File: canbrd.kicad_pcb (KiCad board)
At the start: 2 copper layers, 100 x 100 mm, 219 parts, among them J1 RP_DEBUG, J10 PwrOut, J11 IO2, J12 I^{2}C, J13 USB_C_Receptacle, J14 IO1, J15 IO0, J2 UPDI, J3 Micro_SD_Card, J4 GND, J5 Field24V, J6 Amphenol RJHSE5380, J7 Amphenol RJHSE5380, J8 CAN, J9 CAN, Q1 2N7002K, Q2 BSS83P, Q3 BSS83P, Q4 Q_PMOS_GDS, Q5 BC856, SW1 BOOTSEL, SW2 RESET, SW3 SW_DIP_x08, SW4 User, U1 W25Q16JVSNIQ, U10 ULN2003A, U11 ULN2003A, U12 MAX17634BATP+, U13 AP62250WU, U2 RP2040, U3 TJA1051T-3, U4 MCP2510-x/SO, U5 MAX3485CSA, U6 157119S12801, U8 157119S12801, U9 ATtiny427, Y1 12MHz, Y2 16MHz

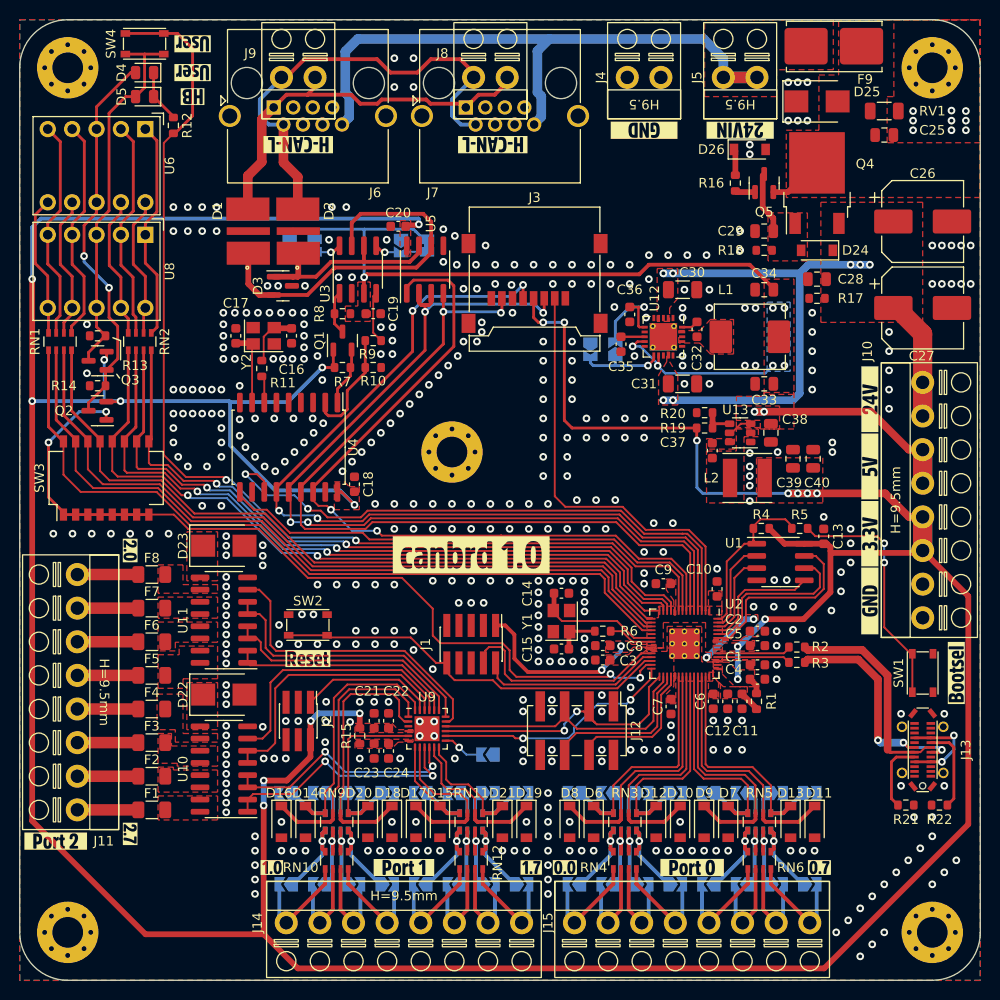
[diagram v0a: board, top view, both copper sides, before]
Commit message: rev1.1: Add I2C pullups
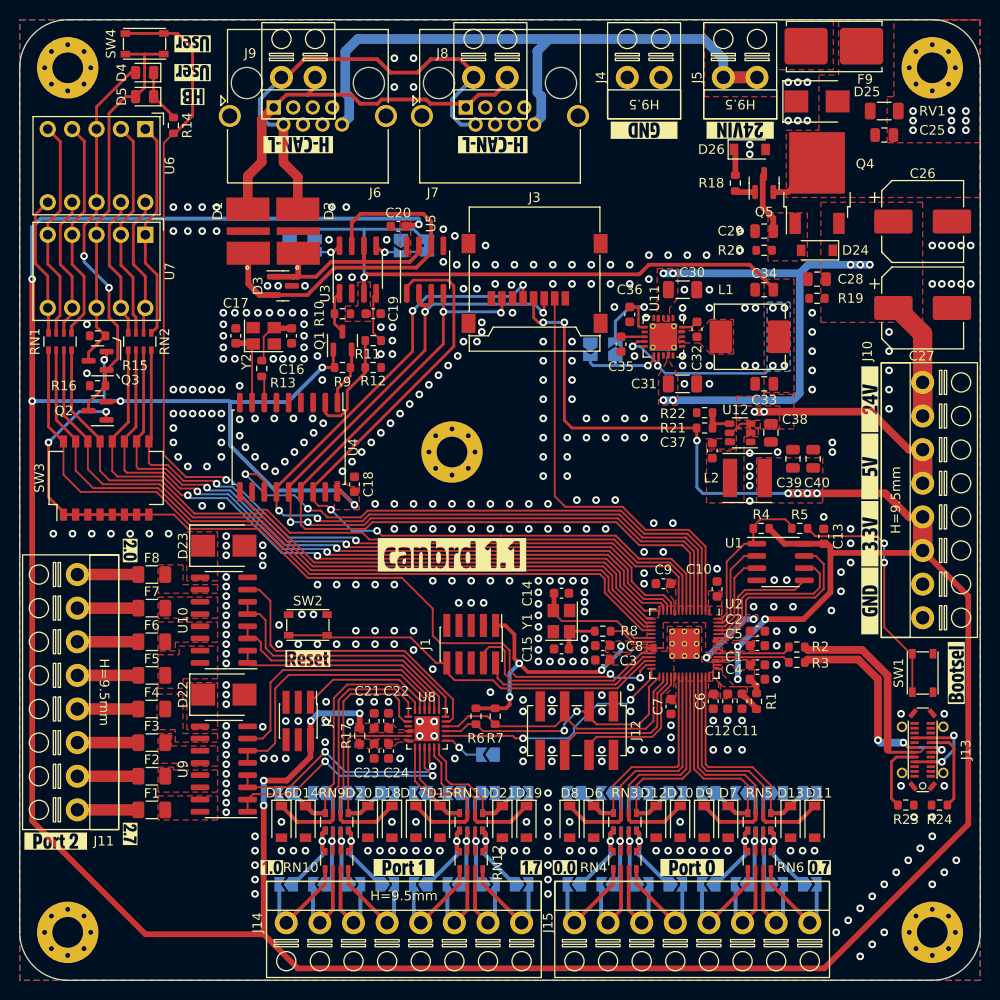
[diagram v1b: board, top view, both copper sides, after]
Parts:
- removed kibuzzard-621788DF: G***, kibuzzard-621788DF
- added R6: 4k7, Resistor_SMD:R_0603_1608Metric, F.Cu at (147.5, 122.5)
- added R7: 4k7, Resistor_SMD:R_0603_1608Metric, F.Cu at (149.5, 122.5)
- added kibuzzard-6234FB7E: G***, kibuzzard-6234FB7E, F.Cu at (145.0, 105.7)
- renumbered R8 to R10, R9 to R11, R10 to R12, R11 to R13, R12 to R14, R13 to R15, R14 to R16, R15 to R17, R16 to R18, R17 to R19, R18 to R20, R19 to R21, R20 to R22, R21 to R23, R22 to R24, R6 to R8, R7 to R9, U11 to U10, U12 to U11, U13 to U12, U8 to U7, U9 to U8, U10 to U9
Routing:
- net +3V3: track 470.6 -> 479.0 mm, vias 23 -> 25
- net /Connectors/SCL: track 30.1 -> 31.0 mm
- net /Connectors/SDA: track 29.7 -> 30.3 mm
- net GND: vias 469 -> 470
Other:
- board text added: "Changelog: rev1.1: Add I2C pullups."
